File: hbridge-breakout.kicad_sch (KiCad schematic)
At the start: 14 parts, among them J1 Conn_01x10, J2 Conn_01x04, J3 Conn_01x08, U1 74HC00, U2 DRV8870DDA

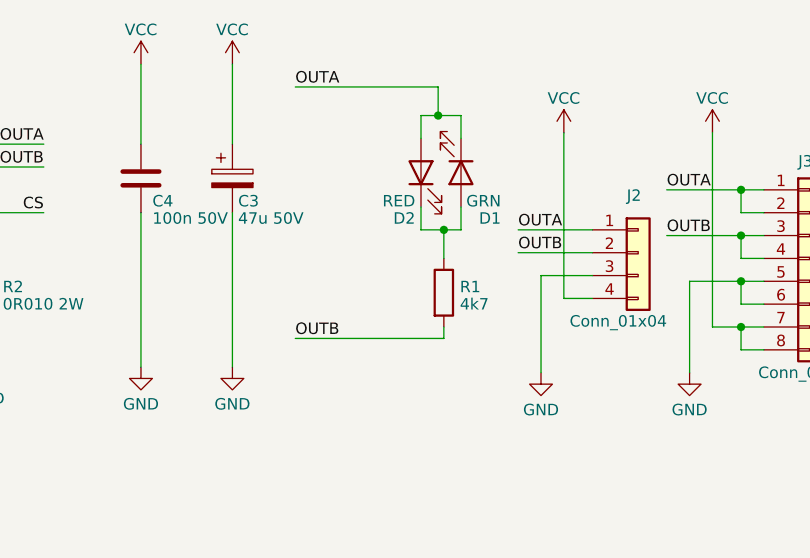
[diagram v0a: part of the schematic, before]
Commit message: Each direction LED now has its own dropper resistor.
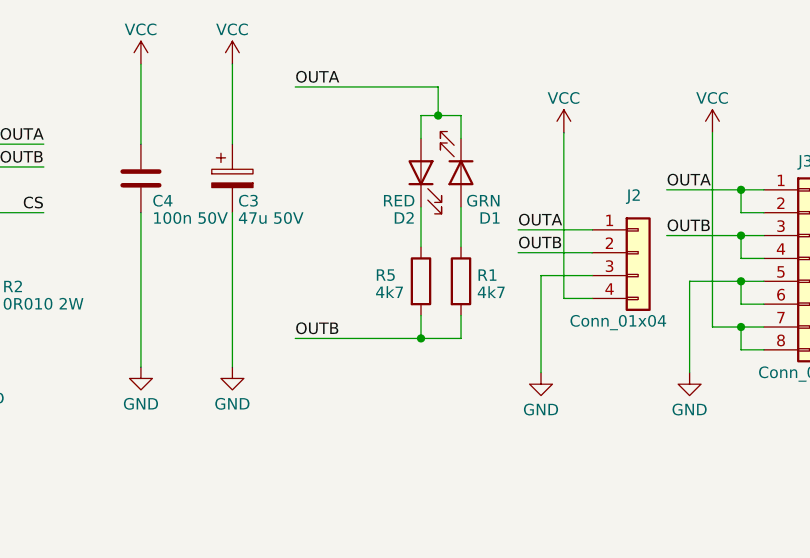
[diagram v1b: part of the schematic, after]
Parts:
- added R5: 4k7, Resistor_SMD:R_0805_2012Metric_Pad1.20x1.40mm_HandSolder, symbol Device:R
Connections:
- net OUTB: now also R5.2
- net at D1.2 (A), R1.1: no longer D2.1 (K)
- new net: D2.1 (K), R5.1
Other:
- moved on the sheet: R1
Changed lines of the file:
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@@
   (junction (at 267.335 74.295) (diameter 0) (color 0 0 0 0)
   )
-  (junction (at 234.315 78.74) (diameter 0) (color 0 0 0 0)
-  )
   (junction (at 74.93 90.805) (diameter 0) (color 0 0 0 0)
   )
@@
   )
   (junction (at 267.335 79.375) (diameter 0) (color 0 0 0 0)
+  )
+  (junction (at 231.775 90.805) (diameter 0) (color 0 0 0 0)
   )
   (junction (at 267.335 84.455) (diameter 0) (color 0 0 0 0)
@@
     (stroke (width 0) (type default))
   )
-  (wire (pts (xy 231.775 76.2) (xy 231.775 78.74))
+  (wire (pts (xy 231.775 76.2) (xy 231.775 80.645))
     (stroke (width 0) (type default))
   )
@@
     (stroke (width 0) (type default))
   )
-  (wire (pts (xy 234.315 78.74) (xy 234.315 81.915))
-    (stroke (width 0) (type default))
-  )
   (wire (pts (xy 150.495 71.755) (xy 158.75 71.755))
     (stroke (width 0) (type default))
@@
     (stroke (width 0) (type default))
   )
-  (wire (pts (xy 236.22 76.2) (xy 236.22 78.74))
+  (wire (pts (xy 236.22 76.2) (xy 236.22 80.645))
     (stroke (width 0) (type default))
   )
@@
     (stroke (width 0) (type default))
   )
-  (wire (pts (xy 236.22 78.74) (xy 234.315 78.74))
-    (stroke (width 0) (type default))
-  )
   (wire (pts (xy 179.07 69.215) (xy 189.865 69.215))
     (stroke (width 0) (type default))
@@
     (stroke (width 0) (type default))
   )
+  (wire (pts (xy 231.775 90.805) (xy 236.22 90.805))
+    (stroke (width 0) (type default))
+  )
   (wire (pts (xy 267.335 89.535) (xy 264.16 89.535))
     (stroke (width 0) (type default))
@@
     (stroke (width 0) (type default))
   )
-  (wire (pts (xy 217.805 90.805) (xy 234.315 90.805))
+  (wire (pts (xy 217.805 90.805) (xy 231.775 90.805))
     (stroke (width 0) (type default))
   )
@@
     (stroke (width 0) (type default))
   )
-  (wire (pts (xy 234.315 89.535) (xy 234.315 90.805))
+  (wire (pts (xy 236.22 88.265) (xy 236.22 90.805))
     (stroke (width 0) (type default))
   )
@@
     (stroke (width 0) (type default))
   )
-  (wire (pts (xy 231.775 78.74) (xy 234.315 78.74))
-    (stroke (width 0) (type default))
-  )
   (wire (pts (xy 136.525 60.325) (xy 136.525 76.835))
     (stroke (width 0) (type default))
@@
   )
   (wire (pts (xy 200.66 60.325) (xy 200.66 69.215))
+    (stroke (width 0) (type default))
+  )
+  (wire (pts (xy 231.775 88.265) (xy 231.775 90.805))
     (stroke (width 0) (type default))
   )
@@
     )
   )
-  (symbol (lib_id "Device:R") (at 234.315 85.725 0) (unit 1)
-    (in_bom yes) (on_board yes) (dnp no) (fields_autoplaced)
-    (property "Reference" "R1" (at 236.093 85.0813 0)
-      (effects (font (size 1.27 1.27)) (justify left))
-    )
-    (property "Value" "4k7" (at 236.093 87.0023 0)
-      (effects (font (size 1.27 1.27)) (justify left))
-    )
-    (property "Footprint" "Resistor_SMD:R_0805_2012Metric_Pad1.20x1.40mm_HandSolder" (at 232.537 85.725 90)
-      (effects (font (size 1.27 1.27)) hide)
-    )
-    (property "Datasheet" "~" (at 234.315 85.725 0)
+  (symbol (lib_id "Device:R") (at 236.22 84.455 0) (unit 1)
+    (in_bom yes) (on_board yes) (dnp no) (fields_autoplaced)
+    (property "Reference" "R1" (at 237.998 83.8113 0)
+      (effects (font (size 1.27 1.27)) (justify left))
+    )
+    (property "Value" "4k7" (at 237.998 85.7323 0)
+      (effects (font (size 1.27 1.27)) (justify left))
+    )
+    (property "Footprint" "Resistor_SMD:R_0805_2012Metric_Pad1.20x1.40mm_HandSolder" (at 234.442 84.455 90)
+      (effects (font (size 1.27 1.27)) hide)
+    )
+    (property "Datasheet" "~" (at 236.22 84.455 0)
       (effects (font (size 1.27 1.27)) hide)
     )
@@
         )
       )
+    )
+  )
+  (symbol (lib_id "Device:R") (at 231.775 84.455 0) (unit 1)
+    (in_bom yes) (on_board yes) (dnp no)
+    (property "Reference" "R5" (at 226.695 83.804 0)
+      (effects (font (size 1.27 1.27)) (justify left))
+    )
+    (property "Value" "4k7" (at 226.695 85.725 0)
+      (effects (font (size 1.27 1.27)) (justify left))
+    )
+    (property "Footprint" "Resistor_SMD:R_0805_2012Metric_Pad1.20x1.40mm_HandSolder" (at 229.997 84.455 90)
+      (effects (font (size 1.27 1.27)) hide)
+    )
+    (property "Datasheet" "~" (at 231.775 84.455 0)
+      (effects (font (size 1.27 1.27)) hide)
+    )
+    (pin "1")
+    (pin "2")
+    (instances
+      (project "hbridge-breakout"
+        (path "/0ad412d3-9893-4dc0-b6f9-32499d04c490"
+          (reference "R5") (unit 1)
+        )
+      )

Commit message: Add note to try DRV8251
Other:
- note added: "Consider trying DRV8251"
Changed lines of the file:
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@@
     (stroke (width 0) (type default))
+  )
+  (text "Consider trying DRV8251\n" (at 156.845 103.505 0)
+    (effects (font (size 1.27 1.27)) (justify left bottom))
   )
   (text "Inspired by https://www.pololu.com/product/1451/pictures"
